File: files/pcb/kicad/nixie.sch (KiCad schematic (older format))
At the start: 13 parts, among them IC2 IC_16PIN, IC3 IC_4PIN, IC4 IC_4PIN, IC5 SN74141_K155NA, IC6 TLP627-4, IC7 TLP627-4

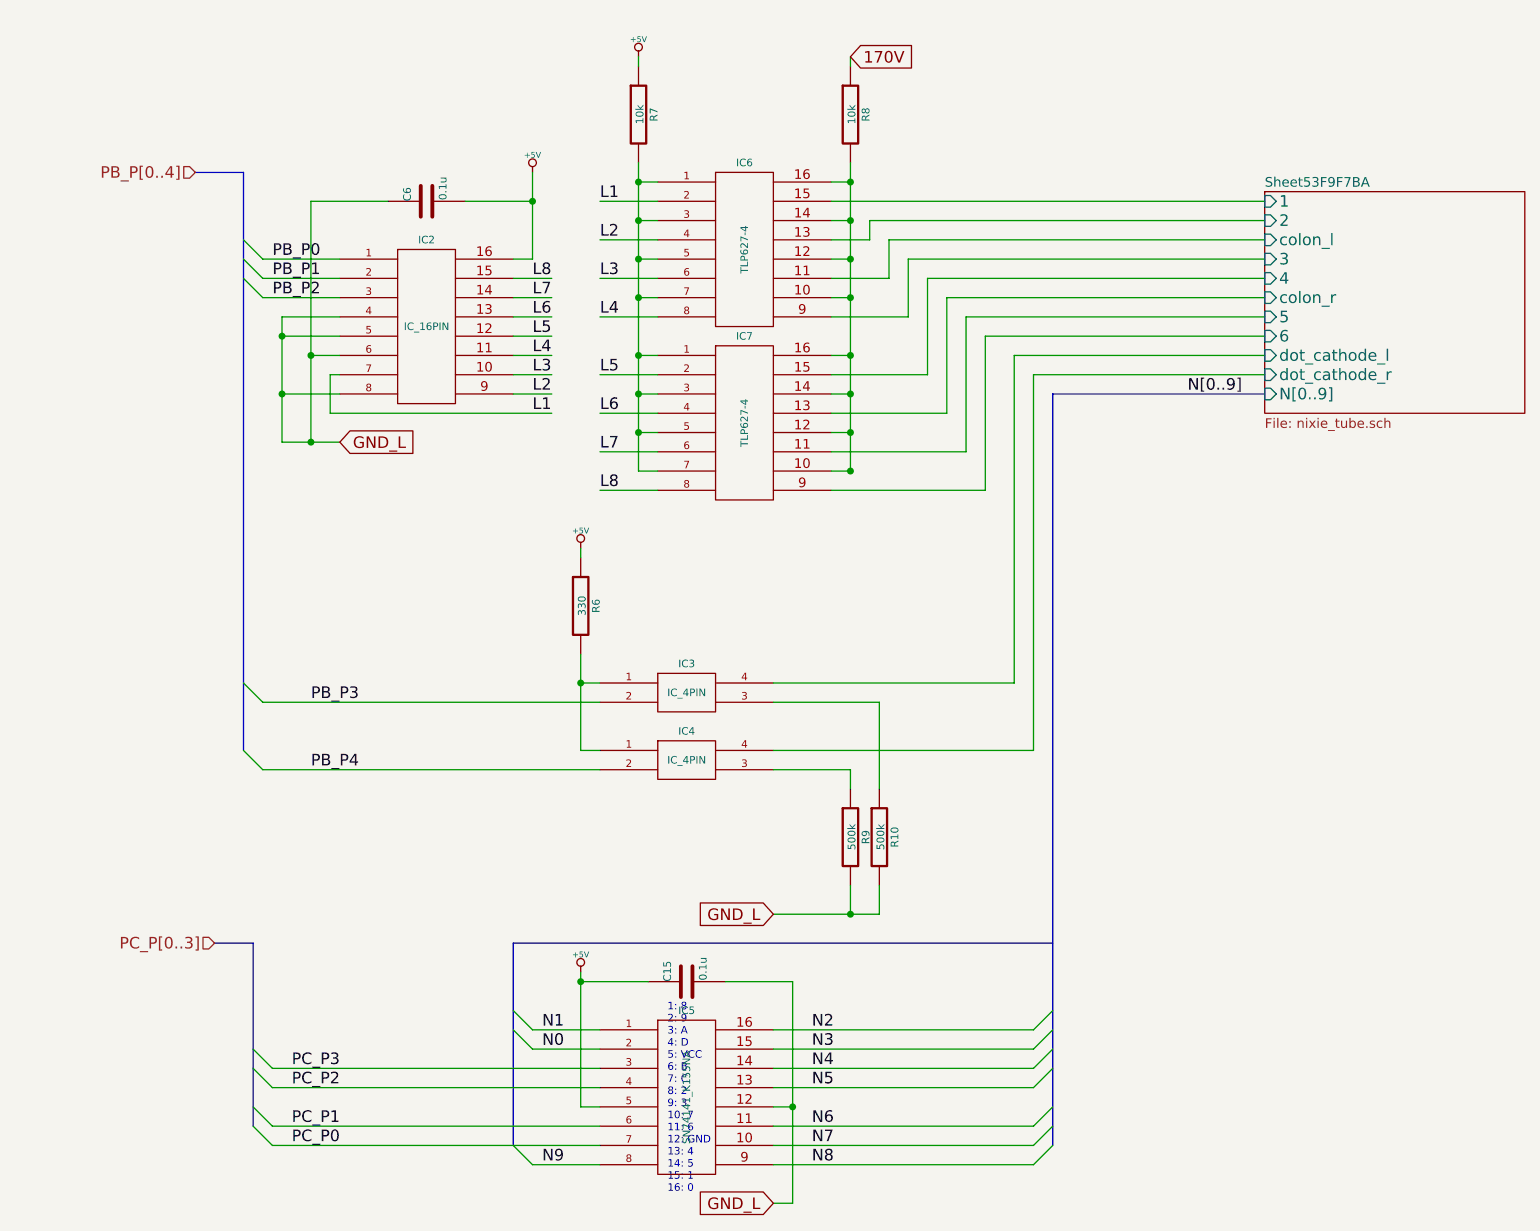
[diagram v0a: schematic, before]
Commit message: 設計見直し
部品見直し
USB・DCジャック自動切り替え
マイコンを下段のボードに移動
ニキシー管駆動電源を上段ボードに移動
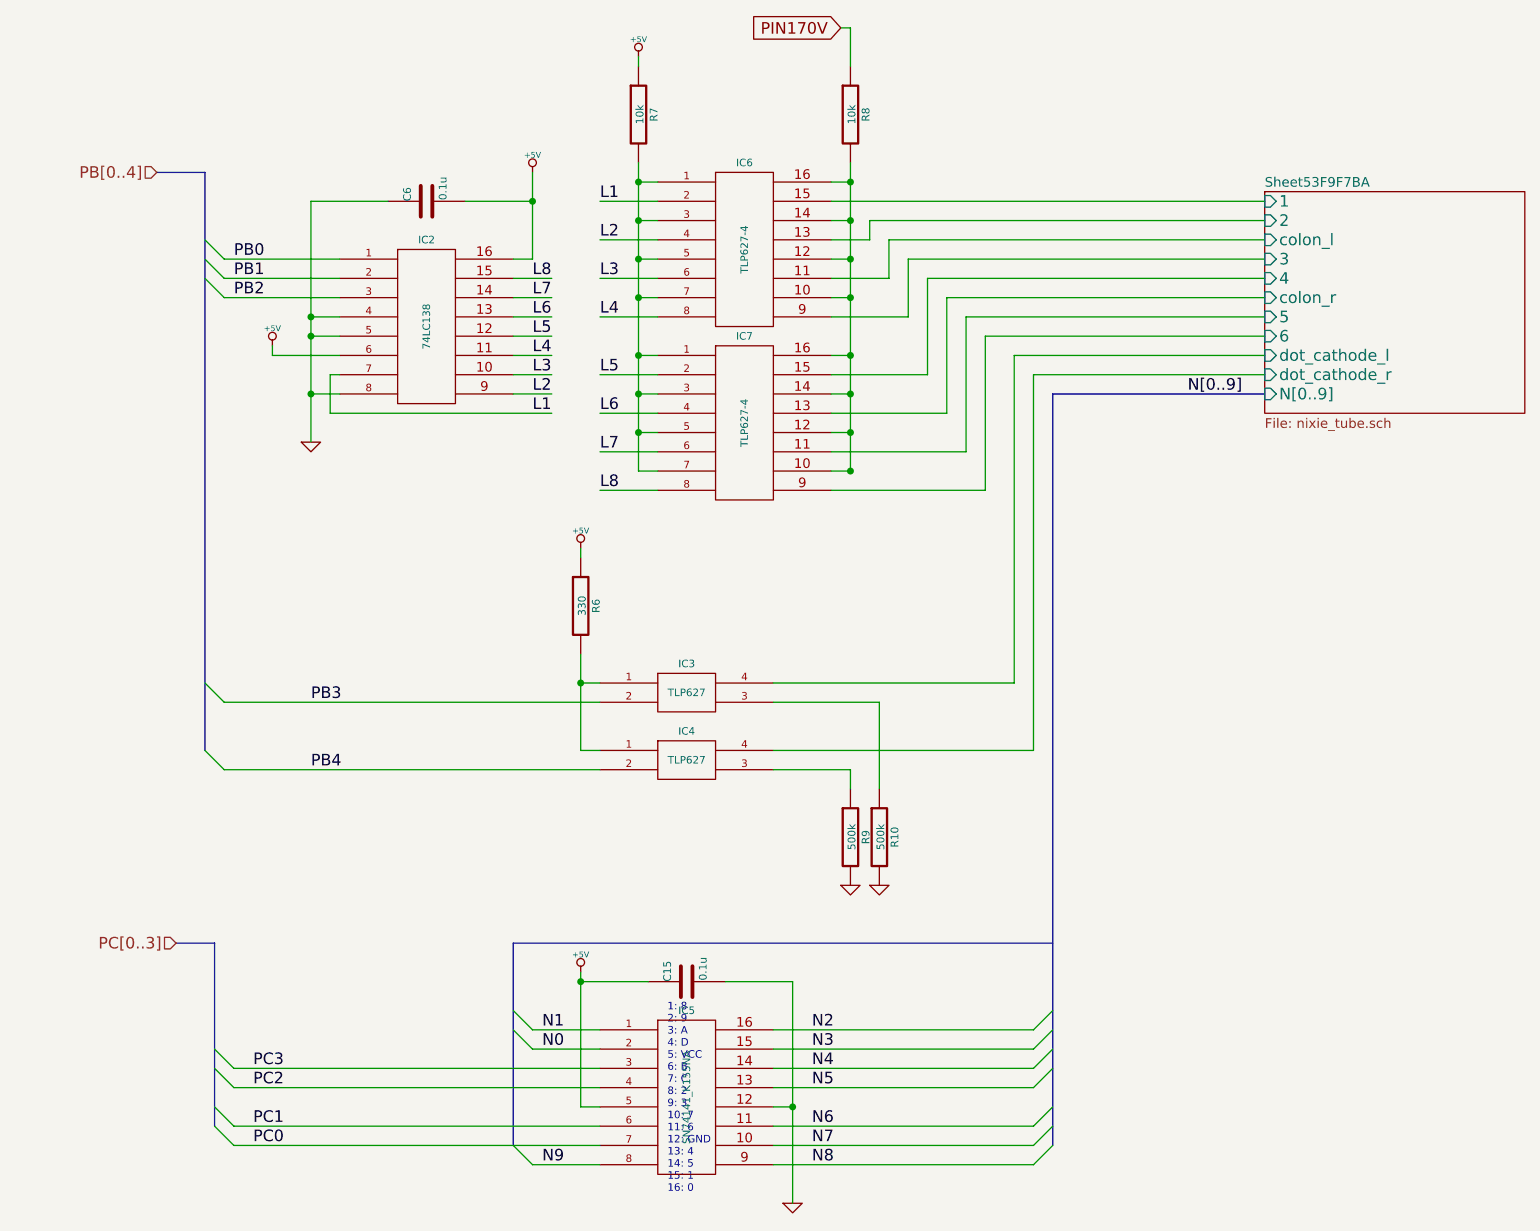
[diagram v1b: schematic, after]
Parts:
- IC2: value IC_16PIN -> 74LC138
- IC3, IC4: value IC_4PIN -> TLP627
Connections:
- net labels added: GND, PB0, PB1, PB2, PB3, PB4, PB[0..4], PC0, PC1, PC2, PC3, PC[0..3], PIN170V
- net labels removed: 170V, GND_L, PB_P0, PB_P1, PB_P2, PB_P3, PB_P4, PB_P[0..4], PC_P0, PC_P1, PC_P2, PC_P3, PC_P[0..3]
- wire segments 116 -> 112
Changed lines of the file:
@@
 $Descr A4 11693 8268
 encoding utf-8
-Sheet 2 11
+Sheet 2 8
 Title ""
-Date "31 aug 2014"
+Date "1 sep 2014"
 Rev ""
 Comp ""
@@
 Comment4 ""
 $EndDescr
-Text HLabel 2250 1450 0    60   Input ~ 0
-PB_P[0..4]
+Text HLabel 2050 1450 0    60   Input ~ 0
+PB[0..4]
 $Comp
 L IC_16PIN IC5
@@
 1: 8\n2: 9\n3: A \n4: D\n5: VCC\n6: B\n7: C\n8: 2\n9: 3\n10: 7\n11: 6\n12: GND\n13: 4\n14: 5\n15: 1\n16: 0
 Entry Wire Line
-	2550 6000 2650 6100
-Entry Wire Line
-	2550 6100 2650 6200
-Entry Wire Line
-	2550 6300 2650 6400
-Entry Wire Line
-	2550 6400 2650 6500
-$Comp
-L +5V #PWR017
+	2350 6000 2450 6100
+Entry Wire Line
+	2350 6100 2450 6200
+Entry Wire Line
+	2350 6300 2450 6400
+Entry Wire Line
+	2350 6400 2450 6500
+$Comp
+L +5V #PWR018
 U 1 1 53F99ADE
 P 4250 5600
-F 0 "#PWR017" H 4250 5690 20  0001 C CNN
+F 0 "#PWR018" H 4250 5690 20  0001 C CNN
 F 1 "+5V" H 4250 5690 30  0000 C CNN
 F 2 "" H 4250 5600 60  0000 C CNN
@@
 Entry Wire Line
 	6600 6600 6700 6500
-$Comp
-L +5V #PWR018
-U 1 1 53F99C3B
-P 4000 1450
-F 0 "#PWR018" H 4000 1540 20  0001 C CNN
-F 1 "+5V" H 4000 1540 30  0000 C CNN
-F 2 "" H 4000 1450 60  0000 C CNN
-F 3 "" H 4000 1450 60  0000 C CNN
-	1    4000 1450
-	1    0    0    -1
-$EndComp
-Entry Wire Line
-	2500 1800 2600 1900
-Entry Wire Line
-	2500 1900 2600 2000
-Entry Wire Line
-	2500 2000 2600 2100
-$Comp
-L +5V #PWR019
-U 1 1 53F99CF6
-P 4550 850
-F 0 "#PWR019" H 4550 940 20  0001 C CNN
-F 1 "+5V" H 4550 940 30  0000 C CNN
-F 2 "" H 4550 850 60  0000 C CNN
-F 3 "" H 4550 850 60  0000 C CNN
-	1    4550 850
-	1    0    0    -1
-$EndComp
+Entry Wire Line
+	2300 1800 2400 1900
+Entry Wire Line
+	2300 1900 2400 2000
+Entry Wire Line
+	2300 2000 2400 2100
 $Comp
 L R R7
@@
 P 4800 4500
 F 0 "IC4" H 4800 4650 39  0000 C CNN
-F 1 "IC_4PIN" H 4800 4500 39  0000 C CNN
+F 1 "TLP627" H 4800 4500 39  0000 C CNN
 F 2 "~" H 4750 4350 60  0000 C CNN
 F 3 "~" H 4750 4350 60  0000 C CNN
@@
 P 4800 4150
 F 0 "IC3" H 4800 4300 39  0000 C CNN
-F 1 "IC_4PIN" H 4800 4150 39  0000 C CNN
+F 1 "TLP627" H 4800 4150 39  0000 C CNN
 F 2 "~" H 4750 4000 60  0000 C CNN
 F 3 "~" H 4750 4000 60  0000 C CNN
 	1    4800 4150
-	1    0    0    -1
-$EndComp
-$Comp
-L +5V #PWR020
-U 1 1 53FAC041
-P 4250 3400
-F 0 "#PWR020" H 4250 3490 20  0001 C CNN
-F 1 "+5V" H 4250 3490 30  0000 C CNN
-F 2 "" H 4250 3400 60  0000 C CNN
-F 3 "" H 4250 3400 60  0000 C CNN
-	1    4250 3400
 	1    0    0    -1
 $EndComp
@@
 $EndComp
 Entry Wire Line
-	2500 4100 2600 4200
-Entry Wire Line
-	2500 4450 2600 4550
-Text HLabel 2350 5450 0    60   Input ~ 0
-PC_P[0..3]
-Text Label 2650 1900 0    60   ~ 0
-PB_P0
-Text Label 2650 2000 0    60   ~ 0
-PB_P1
-Text Label 2650 2100 0    60   ~ 0
-PB_P2
-Text Label 2750 6100 0    60   ~ 0
-PC_P3
-Text Label 2750 6500 0    60   ~ 0
-PC_P0
-Text Label 2750 6400 0    60   ~ 0
-PC_P1
-Text Label 2750 6200 0    60   ~ 0
-PC_P2
+	2300 4100 2400 4200
+Entry Wire Line
+	2300 4450 2400 4550
+Text HLabel 2150 5450 0    60   Input ~ 0
+PC[0..3]
+Text Label 2450 1900 0    60   ~ 0
+PB0
+Text Label 2450 2000 0    60   ~ 0
+PB1
+Text Label 2450 2100 0    60   ~ 0
+PB2
+Text Label 2550 6100 0    60   ~ 0
+PC3
+Text Label 2550 6500 0    60   ~ 0
+PC0
+Text Label 2550 6400 0    60   ~ 0
+PC1
+Text Label 2550 6200 0    60   ~ 0
+PC2
 Text Label 4050 6000 0    60   ~ 0
 N0
@@
 N9
 Text Label 2850 4200 0    60   ~ 0
-PB_P3
+PB3
 Text Label 2850 4550 0    60   ~ 0
-PB_P4
+PB4
 Text Label 7400 2600 0    60   ~ 0
 N[0..9]
@@
 P 3450 2250
 F 0 "IC2" H 3450 2700 39  0000 C CNN
-F 1 "IC_16PIN" H 3450 2250 39  0000 C CNN
+F 1 "74LC138" V 3450 2250 39  0000 C CNN
 F 2 "~" H 3650 1850 60  0000 C CNN
 F 3 "~" H 3650 1850 60  0000 C CNN
@@
 	0    -1   -1   0
 $EndComp
-Text GLabel 5650 850  2    60   Input ~ 0
-170V
+Text GLabel 5600 700  0    60   Input ~ 0
+PIN170V
 Wire Wire Line
 	4550 850  4550 850
@@
 	4550 850  4550 900
 Wire Bus Line
-	2500 1450 2250 1450
-Wire Bus Line
-	2500 1450 2500 4450
-Wire Wire Line
-	2600 1900 3000 1900
-Wire Wire Line
-	2600 2000 3000 2000
-Wire Wire Line
-	2600 2100 3000 2100
+	2300 1450 2050 1450
+Wire Bus Line
+	2300 1450 2300 4450
+Wire Wire Line
+	2400 1900 3000 1900
+Wire Wire Line
+	2400 2000 3000 2000
+Wire Wire Line
+	2400 2100 3000 2100
 Wire Wire Line
 	4000 1450 4000 1900
-Wire Wire Line
-	3000 2400 2850 2400
-Connection ~ 2700 2300
-Wire Wire Line
-	3000 2300 2700 2300
-Wire Wire Line
-	2700 2200 2700 2850
-Wire Wire Line
-	3000 2200 2700 2200
+Connection ~ 2850 2300
+Wire Wire Line
+	2850 2300 3000 2300
+Wire Wire Line
+	2850 1600 2850 2850
+Wire Wire Line
+	3000 2200 2850 2200
 Wire Wire Line
 	5250 5900 6600 5900
@@
 	4250 6300 4350 6300
 Wire Wire Line
-	2650 6500 4350 6500
-Wire Wire Line
-	2650 6400 4350 6400
-Wire Wire Line
-	2650 6200 4350 6200
-Wire Wire Line
-	2650 6100 4350 6100
+	2450 6500 4350 6500
+Wire Wire Line
+	2450 6400 4350 6400
+Wire Wire Line
+	2450 6200 4350 6200
+Wire Wire Line
+	2450 6100 4350 6100
 Wire Wire Line
 	4350 3100 4650 3100
@@
 	5650 1400 5650 3000
 Wire Wire Line
-	5650 850  5650 900
+	5600 700  5650 700
 Wire Wire Line
 	5650 1700 5550 1700
@@
 	6350 2300 7800 2300
 Wire Wire Line
-	5650 5150 5650 5300
-Wire Wire Line
 	6150 2100 7800 2100
 Wire Wire Line
@@
 Connection ~ 4250 4100
 Wire Wire Line
-	4350 4550 2600 4550
-Wire Wire Line
-	4350 4200 2600 4200
+	4350 4550 2400 4550
+Wire Wire Line
+	4350 4200 2400 4200
 Wire Wire Line
 	5650 4550 5250 4550
@@
 	5800 4200 5800 4650
 Wire Bus Line
-	2550 5450 2550 6400
-Wire Bus Line
-	2550 5450 2350 5450
+	2350 5450 2350 6400
+Wire Bus Line
+	2350 5450 2150 5450
 Wire Bus Line
 	6700 2600 7800 2600
@@
 	6700 2600 6700 6500
 Wire Wire Line
-	3000 2600 2700 2600
-Connection ~ 2700 2600
-Wire Wire Line
-	2850 1600 2850 2850
-Connection ~ 2850 2400
+	3000 2600 2850 2600
+Connection ~ 2850 2600
 Wire Wire Line
 	3000 2500 2950 2500
 Wire Wire Line
 	2950 2500 2950 2700
-Wire Wire Line
-	5800 5150 5800 5300
 Wire Wire Line
 	6600 2500 6600 4450
@@
 Connection ~ 4000 1600
 Wire Wire Line
-	3250 1600 2850 1600
+	2850 1600 3250 1600
 Text Label 4000 2700 0    60   ~ 0
 L1
@@
 Text Label 4350 3100 0    60   ~ 0
 L8
-Text GLabel 5250 5300 0    60   Input ~ 0
-GND_L
-Wire Wire Line
-	5800 5300 5250 5300
-Connection ~ 5650 5300
-Text GLabel 5250 6800 0    60   Input ~ 0
-GND_L
-Text GLabel 3000 2850 2    60   Input ~ 0
-GND_L
-Wire Wire Line
-	2700 2850 3000 2850
-Connection ~ 2850 2850
-Wire Wire Line
-	5350 6800 5250 6800
+$Comp
+L +5V #PWR019
+U 1 1 53F99CF6
+P 4550 850
+F 0 "#PWR019" H 4550 940 20  0001 C CNN
+F 1 "+5V" H 4550 940 30  0000 C CNN
+F 2 "" H 4550 850 60  0000 C CNN
+F 3 "" H 4550 850 60  0000 C CNN
+	1    4550 850
+	1    0    0    -1
+$EndComp
+$Comp
+L +5V #PWR020
+U 1 1 53F99C3B
+P 4000 1450
+F 0 "#PWR020" H 4000 1540 20  0001 C CNN
+F 1 "+5V" H 4000 1540 30  0000 C CNN
+F 2 "" H 4000 1450 60  0000 C CNN
+F 3 "" H 4000 1450 60  0000 C CNN
+	1    4000 1450
+	1    0    0    -1
+$EndComp
+$Comp
+L +5V #PWR021
+U 1 1 53FAC041
+P 4250 3400
+F 0 "#PWR021" H 4250 3490 20  0001 C CNN
+F 1 "+5V" H 4250 3490 30  0000 C CNN
+F 2 "" H 4250 3400 60  0000 C CNN
+F 3 "" H 4250 3400 60  0000 C CNN
+	1    4250 3400
+	1    0    0    -1
+$EndComp
+Wire Wire Line
+	5650 700  5650 900
+$Comp
+L GND #PWR022
+U 1 1 5404D8B8
+P 5650 5150
+F 0 "#PWR022" H 5650 5150 30  0001 C CNN
+F 1 "GND" H 5650 5080 30  0001 C CNN
+F 2 "" H 5650 5150 60  0000 C CNN
+F 3 "" H 5650 5150 60  0000 C CNN
+	1    5650 5150
+	1    0    0    -1
+$EndComp
+$Comp
+L GND #PWR023
+U 1 1 5404D8C7
+P 5800 5150
+F 0 "#PWR023" H 5800 5150 30  0001 C CNN
+F 1 "GND" H 5800 5080 30  0001 C CNN
+F 2 "" H 5800 5150 60  0000 C CNN
+F 3 "" H 5800 5150 60  0000 C CNN
+	1    5800 5150
+	1    0    0    -1
+$EndComp
+$Comp
+L GND #PWR024
+U 1 1 5404D95A
+P 5350 6800
+F 0 "#PWR024" H 5350 6800 30  0001 C CNN
+F 1 "GND" H 5350 6730 30  0001 C CNN
+F 2 "" H 5350 6800 60  0000 C CNN
+F 3 "" H 5350 6800 60  0000 C CNN
+	1    5350 6800
+	1    0    0    -1
+$EndComp
+$Comp
+L GND #PWR025
+U 1 1 5404DA3E
+P 2850 2850
+F 0 "#PWR025" H 2850 2850 30  0001 C CNN
+F 1 "GND" H 2850 2780 30  0001 C CNN
+F 2 "" H 2850 2850 60  0000 C CNN
+F 3 "" H 2850 2850 60  0000 C CNN
+	1    2850 2850
+	1    0    0    -1
+$EndComp
+Wire Wire Line
+	2650 2400 3000 2400
+Wire Wire Line
+	2650 2350 2650 2400
+Connection ~ 2850 2200
+$Comp
+L +5V #PWR026
+U 1 1 5404E099
+P 2650 2350
+F 0 "#PWR026" H 2650 2440 20  0001 C CNN
+F 1 "+5V" H 2650 2440 30  0000 C CNN
+F 2 "" H 2650 2350 60  0000 C CNN
+F 3 "" H 2650 2350 60  0000 C CNN
+	1    2650 2350
+	1    0    0    -1
+$EndComp
 $EndSCHEMATC

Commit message: 基板が描けた
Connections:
- net labels added: PINPB0, PINPB1, PINPB2, PINPB3, PINPB4, PINPB[0..4], PINPC0, PINPC1, PINPC2, PINPC3, PINPC[0..3]
- net labels removed: PB0, PB1, PB2, PB3, PB4, PB[0..4], PC0, PC1, PC2, PC3, PC[0..3]
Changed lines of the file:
@@
 Sheet 2 8
 Title ""
-Date "4 sep 2014"
+Date "5 sep 2014"
 Rev ""
 Comp ""
@@
 $EndDescr
 Text HLabel 2050 1450 0    60   Input ~ 0
-PB[0..4]
+PINPB[0..4]
 $Comp
 L IC_16PIN IC5
@@
 	2350 6400 2450 6500
 $Comp
-L +5V #PWR019
+L +5V #PWR010
 U 1 1 53F99ADE
 P 4250 5600
-F 0 "#PWR019" H 4250 5690 20  0001 C CNN
+F 0 "#PWR010" H 4250 5690 20  0001 C CNN
 F 1 "+5V" H 4250 5690 30  0000 C CNN
 F 2 "" H 4250 5600 60  0000 C CNN
@@
 	2300 4450 2400 4550
 Text HLabel 2150 5450 0    60   Input ~ 0
-PC[0..3]
+PINPC[0..3]
 Text Label 2450 1900 0    60   ~ 0
-PB0
+PINPB0
 Text Label 2450 2000 0    60   ~ 0
-PB1
+PINPB1
 Text Label 2450 2100 0    60   ~ 0
-PB2
+PINPB2
 Text Label 2550 6100 0    60   ~ 0
-PC3
+PINPC3
 Text Label 2550 6500 0    60   ~ 0
-PC0
+PINPC0
 Text Label 2550 6400 0    60   ~ 0
-PC1
+PINPC1
 Text Label 2550 6200 0    60   ~ 0
-PC2
+PINPC2
 Text Label 4050 6000 0    60   ~ 0
 N0
 Text Label 4050 5900 0    60   ~ 0
 N1
+Text Label 5450 6000 0    60   ~ 0
+N2
 Text Label 5450 5900 0    60   ~ 0
-N2
-Text Label 5450 6000 0    60   ~ 0
 N3
+Text Label 5450 6200 0    60   ~ 0
+N4
 Text Label 5450 6100 0    60   ~ 0
-N4
-Text Label 5450 6200 0    60   ~ 0
 N5
-Text Label 5450 6400 0    60   ~ 0
+Text Label 5450 6600 0    60   ~ 0
 N6
 Text Label 5450 6500 0    60   ~ 0
 N7
-Text Label 5450 6600 0    60   ~ 0
+Text Label 5450 6400 0    60   ~ 0
 N8
 Text Label 4050 6600 0    60   ~ 0
 N9
 Text Label 2850 4200 0    60   ~ 0
-PB3
+PINPB3
 Text Label 2850 4550 0    60   ~ 0
-PB4
+PINPB4
 Text Label 7400 2600 0    60   ~ 0
 N[0..9]
@@
 L8
 $Comp
-L +5V #PWR020
+L +5V #PWR011
 U 1 1 53F99CF6
 P 4550 850
-F 0 "#PWR020" H 4550 940 20  0001 C CNN
+F 0 "#PWR011" H 4550 940 20  0001 C CNN
 F 1 "+5V" H 4550 940 30  0000 C CNN
 F 2 "" H 4550 850 60  0000 C CNN
@@
 $EndComp
 $Comp
-L +5V #PWR021
+L +5V #PWR012
 U 1 1 53F99C3B
 P 4000 1450
-F 0 "#PWR021" H 4000 1540 20  0001 C CNN
+F 0 "#PWR012" H 4000 1540 20  0001 C CNN
 F 1 "+5V" H 4000 1540 30  0000 C CNN
 F 2 "" H 4000 1450 60  0000 C CNN
@@
 $EndComp
 $Comp
-L +5V #PWR022
+L +5V #PWR013
 U 1 1 53FAC041
 P 4250 3400
-F 0 "#PWR022" H 4250 3490 20  0001 C CNN
+F 0 "#PWR013" H 4250 3490 20  0001 C CNN
 F 1 "+5V" H 4250 3490 30  0000 C CNN
 F 2 "" H 4250 3400 60  0000 C CNN
@@
 	5650 700  5650 900
 $Comp
-L GND #PWR023
+L GND #PWR014
 U 1 1 5404D8B8
 P 5650 5150
-F 0 "#PWR023" H 5650 5150 30  0001 C CNN
+F 0 "#PWR014" H 5650 5150 30  0001 C CNN
 F 1 "GND" H 5650 5080 30  0001 C CNN
 F 2 "" H 5650 5150 60  0000 C CNN
@@
 $EndComp
 $Comp
-L GND #PWR024
+L GND #PWR015
 U 1 1 5404D8C7
 P 5800 5150
-F 0 "#PWR024" H 5800 5150 30  0001 C CNN
+F 0 "#PWR015" H 5800 5150 30  0001 C CNN
 F 1 "GND" H 5800 5080 30  0001 C CNN
 F 2 "" H 5800 5150 60  0000 C CNN
@@
 $EndComp
 $Comp
-L GND #PWR025
+L GND #PWR016
 U 1 1 5404D95A
 P 5350 6800
-F 0 "#PWR025" H 5350 6800 30  0001 C CNN
+F 0 "#PWR016" H 5350 6800 30  0001 C CNN
 F 1 "GND" H 5350 6730 30  0001 C CNN
 F 2 "" H 5350 6800 60  0000 C CNN
@@
 $EndComp
 $Comp
-L GND #PWR026
+L GND #PWR017
 U 1 1 5404DA3E
 P 2850 2850
-F 0 "#PWR026" H 2850 2850 30  0001 C CNN
+F 0 "#PWR017" H 2850 2850 30  0001 C CNN
 F 1 "GND" H 2850 2780 30  0001 C CNN
 F 2 "" H 2850 2850 60  0000 C CNN
@@
 Connection ~ 2850 2200
 $Comp
-L +5V #PWR027
+L +5V #PWR018
 U 1 1 5404E099
 P 2650 2350
-F 0 "#PWR027" H 2650 2440 20  0001 C CNN
+F 0 "#PWR018" H 2650 2440 20  0001 C CNN
 F 1 "+5V" H 2650 2440 30  0000 C CNN
 F 2 "" H 2650 2350 60  0000 C CNN

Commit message: DRC完了
あとはシルク移動かなぁ
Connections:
- wire segments 112 -> 105
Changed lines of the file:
@@
 Sheet 2 8
 Title ""
-Date "5 sep 2014"
+Date "6 sep 2014"
 Rev ""
 Comp ""
@@
 	4350 3100 4650 3100
 Wire Wire Line
-	2950 2700 4100 2700
+	2950 2700 3900 2700
 Wire Wire Line
 	4650 2900 4350 2900
@@
 	4650 2700 4350 2700
 Wire Wire Line
-	4100 2600 3900 2600
-Wire Wire Line
-	4100 2500 3900 2500
-Wire Wire Line
 	4650 2500 4350 2500
 Wire Wire Line
-	4100 2400 3900 2400
-Wire Wire Line
 	4650 2200 4350 2200
 Wire Wire Line
-	4100 2300 3900 2300
-Wire Wire Line
-	3900 2200 4100 2200
-Wire Wire Line
 	4350 2000 4650 2000
 Wire Wire Line
 	4650 1800 4350 1800
-Wire Wire Line
-	4100 2100 3900 2100
-Wire Wire Line
-	3900 2000 4100 2000
 Wire Wire Line
 	4350 1600 4650 1600
@@
 Wire Wire Line
 	2850 1600 3250 1600
-Text Label 4000 2700 0    60   ~ 0
+Text Label 3900 2000 0    60   ~ 0
 L1
-Text Label 4000 2600 0    60   ~ 0
+Text Label 3900 2100 0    60   ~ 0
 L2
-Text Label 4000 2500 0    60   ~ 0
+Text Label 3900 2200 0    60   ~ 0
 L3
-Text Label 4000 2400 0    60   ~ 0
+Text Label 3900 2300 0    60   ~ 0
 L4
-Text Label 4000 2300 0    60   ~ 0
+Text Label 3900 2400 0    60   ~ 0
 L5
-Text Label 4000 2200 0    60   ~ 0
+Text Label 3900 2500 0    60   ~ 0
 L6
-Text Label 4000 2100 0    60   ~ 0
+Text Label 3900 2600 0    60   ~ 0
 L7
-Text Label 4000 2000 0    60   ~ 0
+Text Label 3900 2700 0    60   ~ 0
 L8
 Text Label 4350 1600 0    60   ~ 0
